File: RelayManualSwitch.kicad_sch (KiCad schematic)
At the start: 10 parts

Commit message: 階層基板化中
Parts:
- removed SW?: SW_DPDT_x2, symbol Switch:SW_DPDT_x2
- removed SW?: SW_DPDT_x2, Button_Switch_THT:SW_E-Switch_EG1271_DPDT, symbol Switch:SW_DPDT_x2
- added RN2-1, RN2-2: 2.2k, Resistor_THT:R_Array_SIP9, symbol Device:R_Network08_US
- added SW2-1, SW2-2, SW2-3, SW2-4, SW2-5, SW2-6, SW2-7, SW2-8: SW_SPST, symbol Switch:SW_SPST
- added SW2-9: 2MD1-T2-B4-M2-Q-N, symbol Switch:SW_DPDT_x2
- gave numbers to parts that had none: 8
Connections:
- net OUTPUT1: now also U2-1.6, U2-1.7
- net OUTPUT2: now also U2-2.6, U2-2.7
- net OUTPUT3: now also U2-3.6, U2-3.7
- net OUTPUT5: now also U2-5.6, U2-5.7
- net OUTPUT6: now also U2-6.6, U2-6.7
- net OUTPUT7: now also U2-7.6, U2-7.7
- net OUTPUT8: now also U2-8.6, U2-8.7
- net at U2-4.5: now also SW2-4.1 (A)
- net at U2-4.6: now also U2-4.7
- net at U2-5.5: now also SW2-5.1 (A)
- net at U2-8.5: now also SW2-8.1 (A)
- net at U2-6.5: now also SW2-6.1 (A)
- net at U2-2.5: now also SW2-2.1 (A)
- net at U2-1.5: now also SW2-1.1 (A)
- net at U2-7.5: now also SW2-7.1 (A)
- net at U2-3.5: now also SW2-3.1 (A)
- new net GND: SW2-1.2 (B), SW2-2.2 (B), SW2-3.2 (B), SW2-4.2 (B), SW2-5.2 (B), SW2-6.2 (B), SW2-7.2 (B), SW2-8.2 (B)
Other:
- note added: "P-00301"
- title: (none) -> Relay Control AUTO/MANUAL
- moved on the sheet: U2-1, U2-2, U2-3, U2-4, U2-5, U2-6, U2-7, U2-8

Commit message: 編集
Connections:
- net +5V: now also SW2-9.1 (A), SW2-9.6 (C)
- net GND: now also SW2-9.3 (C), SW2-9.4 (A), U2-1.2, U2-1.4, U2-2.2, U2-2.4, U2-3.2, U2-3.4, U2-4.2, U2-4.4, U2-5.2, U2-5.4, U2-6.2, U2-6.4, U2-7.2, U2-7.4, U2-8.2, U2-8.4
- net INPUT1: now also U2-1.8
- net INPUT2: now also U2-2.8
- net INPUT3: now also U2-3.8
- net INPUT4: now also U2-4.8
- net INPUT5: now also U2-5.8
- net INPUT6: now also U2-6.8
- net INPUT7: now also U2-7.8
- net INPUT8: now also U2-8.8
- net OUTPUT4: now also U2-4.6, U2-4.7
- net at RN2-1.1 (common): now also SW2-9.2 (B)
- net at RN2-1.2 (R1): now also U2-1.3
- net at RN2-1.3 (R2): now also U2-5.3
- net at RN2-1.4 (R3): now also U2-6.3
- net at RN2-1.5 (R4): now also U2-2.3
- net at RN2-1.6 (R5): now also U2-3.3
- net at RN2-1.7 (R6): now also U2-7.3
- net at RN2-1.8 (R7): now also U2-8.3
- net at RN2-1.9 (R8): now also U2-4.3
- net at U2-4.1: now also RN2-2.9 (R8)
- net at U2-5.1: now also RN2-2.3 (R2)
- net at U2-8.1: now also RN2-2.8 (R7)
- net at U2-6.1: now also RN2-2.4 (R3)
- net at U2-2.1: now also RN2-2.5 (R4)
- net at RN2-2.1 (common): now also SW2-9.5 (B)
- net at RN2-2.2 (R1): now also U2-1.1
- net at RN2-2.6 (R5): now also U2-3.1
- net at RN2-2.7 (R6): now also U2-7.1
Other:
- moved on the sheet: RN2-1, RN2-2, SW2-9A, SW2-9B

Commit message: RelayManualSwitch回路充実
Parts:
- added D2-1, D2-2: LED, symbol Device:LED
- added R2-1, R2-2: 510, symbol Device:R_US
- SW2-9: value 2MD1-T2-B4-M2-Q-N -> MS611F
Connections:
- net GND: now also D2-1.1 (K), D2-2.1 (K)
- net at RN2-1.1 (common), SW2-9.2 (B): now also R2-1.1
- net at RN2-2.1 (common), SW2-9.5 (B): now also R2-2.1
- new net: D2-2.2 (A), R2-2.2
- new net: D2-1.2 (A), R2-1.2
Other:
- note added: "AUTO"
- note added: "MANUAL"
- moved on the sheet: SW2-9A, SW2-9B

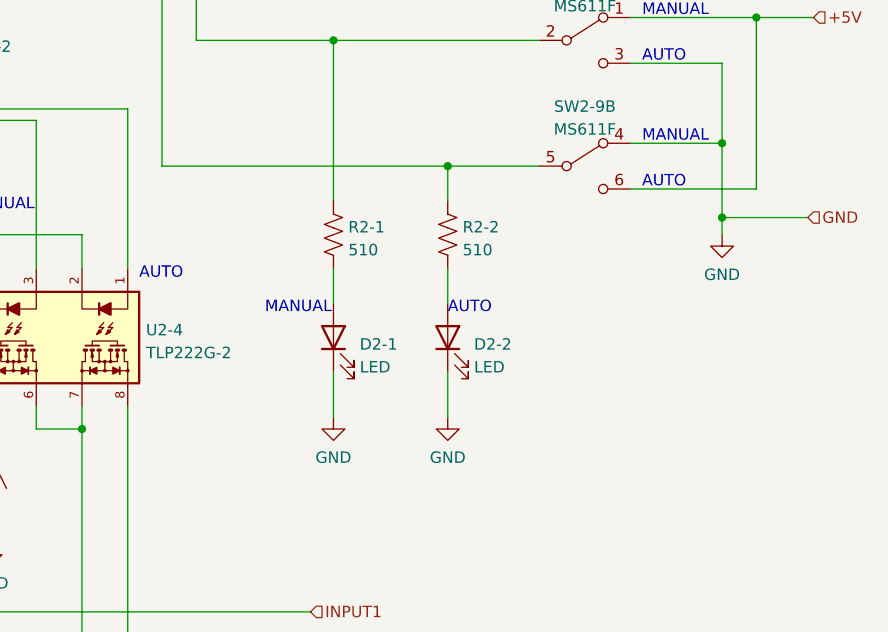
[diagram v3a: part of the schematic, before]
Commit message: Mode STAT monitoring
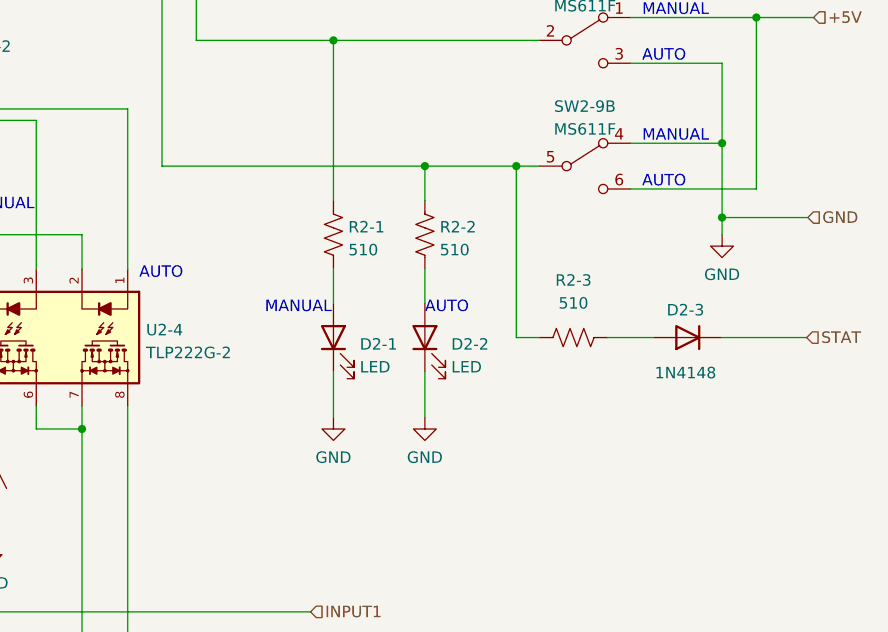
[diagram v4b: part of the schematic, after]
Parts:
- added D2-3: 1N4148, Diode_THT:D_DO-35_SOD27_P7.62mm_Horizontal, symbol Diode:1N4148
- added R2-3: 510, symbol Device:R_US
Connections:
- net at R2-2.1, RN2-2.1 (common), SW2-9.5 (B): now also R2-3.1
- new net: D2-3.2 (A), R2-3.2
- new net STAT: D2-3.1 (K)
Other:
- moved on the sheet: D2-2, R2-2
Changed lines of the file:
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@@
   (junction (at 106.68 76.2) (diameter 0) (color 0 0 0 0)
   )
-  (junction (at 208.28 46.99) (diameter 0) (color 0 0 0 0)
+  (junction (at 205.74 46.99) (diameter 0) (color 0 0 0 0)
   )
   (junction (at 167.64 76.2) (diameter 0) (color 0 0 0 0)
@@
   (junction (at 127 116.84) (diameter 0) (color 0 0 0 0)
   )
+  (junction (at 215.9 46.99) (diameter 0) (color 0 0 0 0)
+  )
   (junction (at 96.52 116.84) (diameter 0) (color 0 0 0 0)
   )
@@
     (stroke (width 0) (type default) (color 0 0 0 0))
   )
+  (wire (pts (xy 238.76 66.04) (xy 248.158 66.04))
+    (stroke (width 0) (type default) (color 0 0 0 0))
+  )
   (wire (pts (xy 146.05 109.22) (xy 132.08 109.22))
     (stroke (width 0) (type default) (color 0 0 0 0))
@@
     (stroke (width 0) (type default) (color 0 0 0 0))
   )
-  (wire (pts (xy 208.28 46.99) (xy 176.53 46.99))
+  (wire (pts (xy 205.74 46.99) (xy 176.53 46.99))
     (stroke (width 0) (type default) (color 0 0 0 0))
   )
@@
     (stroke (width 0) (type default) (color 0 0 0 0))
   )
+  (wire (pts (xy 218.44 66.04) (xy 215.9 66.04))
+    (stroke (width 0) (type default) (color 0 0 0 0))
+  )
   (wire (pts (xy 66.04 118.11) (xy 76.2 118.11))
     (stroke (width 0) (type default) (color 0 0 0 0))
@@
     (stroke (width 0) (type default) (color 0 0 0 0))
   )
+  (wire (pts (xy 215.9 46.99) (xy 205.74 46.99))
+    (stroke (width 0) (type default) (color 0 0 0 0))
+  )
   (wire (pts (xy 95.25 44.45) (xy 146.05 44.45))
     (stroke (width 0) (type default) (color 0 0 0 0))
@@
     (stroke (width 0) (type default) (color 0 0 0 0))
   )
-  (wire (pts (xy 208.28 46.99) (xy 208.28 50.8))
+  (wire (pts (xy 205.74 46.99) (xy 205.74 50.8))
     (stroke (width 0) (type default) (color 0 0 0 0))
   )
@@
     (stroke (width 0) (type default) (color 0 0 0 0))
   )
+  (wire (pts (xy 215.9 66.04) (xy 215.9 46.99))
+    (stroke (width 0) (type default) (color 0 0 0 0))
+  )
   (wire (pts (xy 144.78 39.37) (xy 144.78 57.15))
     (stroke (width 0) (type default) (color 0 0 0 0))
@@
     (stroke (width 0) (type default) (color 0 0 0 0))
   )
+  (wire (pts (xy 226.06 66.04) (xy 231.14 66.04))
+    (stroke (width 0) (type default) (color 0 0 0 0))
+  )
   (wire (pts (xy 167.894 139.7) (xy 167.64 137.16))
     (stroke (width 0) (type default) (color 0 0 0 0))
@@
     (stroke (width 0) (type default) (color 0 0 0 0))
   )
-  (wire (pts (xy 208.28 69.85) (xy 208.28 74.93))
+  (wire (pts (xy 205.74 69.85) (xy 205.74 74.93))
     (stroke (width 0) (type default) (color 0 0 0 0))
   )
@@
     (stroke (width 0) (type default) (color 0 0 0 0))
   )
-  (wire (pts (xy 208.28 58.42) (xy 208.28 62.23))
+  (wire (pts (xy 205.74 58.42) (xy 205.74 62.23))
     (stroke (width 0) (type default) (color 0 0 0 0))
   )
@@
     (stroke (width 0) (type default) (color 0 0 0 0))
   )
-  (wire (pts (xy 218.44 46.99) (xy 208.28 46.99))
+  (wire (pts (xy 218.44 46.99) (xy 215.9 46.99))
     (stroke (width 0) (type default) (color 0 0 0 0))
   )
@@
     (stroke (width 0) (type default) (color 0 0 0 0))
   )
-  (text "AUTO" (at 208.28 63.5 0)
+  (text "AUTO" (at 205.74 63.5 0)
     (effects (font (size 1.27 1.27)) (justify left bottom))
   )
@@
   (hierarchical_label "OUTPUT6" (shape output) (at 50.8 165.1 180)
     (effects (font (size 1.27 1.27)) (justify right))
+  )
+  (hierarchical_label "STAT" (shape input) (at 248.158 66.04 0)
+    (effects (font (size 1.27 1.27)) (justify left))
   )
   (hierarchical_label "OUTPUT2" (shape output) (at 50.8 101.6 180)
@@
     (pin "1")
   )
-  (symbol (lib_id "Device:LED") (at 208.28 66.04 90) (unit 1)
-    (in_bom yes) (on_board yes) (fields_autoplaced)
-    (property "Reference" "D2-2" (id 0) (at 211.201 66.7928 90)
+  (symbol (lib_id "Device:LED") (at 205.74 66.04 90) (unit 1)
+    (in_bom yes) (on_board yes) (fields_autoplaced)
+    (property "Reference" "D2-2" (id 0) (at 208.661 66.7928 90)
       (effects (font (size 1.27 1.27)) (justify right))
     )
-    (property "Value" "LED" (id 1) (at 211.201 69.3297 90)
+    (property "Value" "LED" (id 1) (at 208.661 69.3297 90)
       (effects (font (size 1.27 1.27)) (justify right))
     )
-    (property "Footprint" "" (id 2) (at 208.28 66.04 0)
-      (effects (font (size 1.27 1.27)) hide)
-    )
-    (property "Datasheet" "~" (id 3) (at 208.28 66.04 0)
-      (effects (font (size 1.27 1.27)) hide)
-    )
-    (pin "1")
-    (pin "2")
-  )
-  (symbol (lib_id "Device:R_US") (at 208.28 54.61 0) (unit 1)
-    (in_bom yes) (on_board yes) (fields_autoplaced)
-    (property "Reference" "R2-2" (id 0) (at 209.931 53.7753 0)
-      (effects (font (size 1.27 1.27)) (justify left))
-    )
-    (property "Value" "510" (id 1) (at 209.931 56.3122 0)
-      (effects (font (size 1.27 1.27)) (justify left))
-    )
-    (property "Footprint" "" (id 2) (at 209.296 54.864 90)
-      (effects (font (size 1.27 1.27)) hide)
-    )
-    (property "Datasheet" "~" (id 3) (at 208.28 54.61 0)
+    (property "Footprint" "" (id 2) (at 205.74 66.04 0)
+      (effects (font (size 1.27 1.27)) hide)
+    )
+    (property "Datasheet" "~" (id 3) (at 205.74 66.04 0)
+      (effects (font (size 1.27 1.27)) hide)
+    )
+    (pin "1")
+    (pin "2")
+  )
+  (symbol (lib_id "Device:R_US") (at 205.74 54.61 0) (unit 1)
+    (in_bom yes) (on_board yes) (fields_autoplaced)
+    (property "Reference" "R2-2" (id 0) (at 207.391 53.7753 0)
+      (effects (font (size 1.27 1.27)) (justify left))
+    )
+    (property "Value" "510" (id 1) (at 207.391 56.3122 0)
+      (effects (font (size 1.27 1.27)) (justify left))
+    )
+    (property "Footprint" "" (id 2) (at 206.756 54.864 90)
+      (effects (font (size 1.27 1.27)) hide)
+    )
+    (property "Datasheet" "~" (id 3) (at 205.74 54.61 0)
       (effects (font (size 1.27 1.27)) hide)
     )
@@
     (pin "1")
   )
+  (symbol (lib_id "Diode:1N4148") (at 234.95 66.04 180) (unit 1)
+    (in_bom yes) (on_board yes)
+    (property "Reference" "D2-3" (id 0) (at 234.696 62.992 0))
+    (property "Value" "1N4148" (id 1) (at 234.696 69.977 0))
+    (property "Footprint" "Diode_THT:D_DO-35_SOD27_P7.62mm_Horizontal" (id 2) (at 234.95 61.595 0)
+      (effects (font (size 1.27 1.27)) hide)
+    )
+    (property "Datasheet" "https://assets.nexperia.com/documents/data-sheet/1N4148_1N4448.pdf" (id 3) (at 234.95 66.04 0)
+      (effects (font (size 1.27 1.27)) hide)
+    )
+    (pin "1")
+    (pin "2")
+  )
   (symbol (lib_id "power:GND") (at 91.44 121.92 0) (unit 1)
     (in_bom yes) (on_board yes) (fields_autoplaced)
@@
   (symbol (lib_id "power:GND") (at 195.58 74.93 0) (unit 1)
     (in_bom yes) (on_board yes) (fields_autoplaced)
-    (property "Reference" "#PWR?" (id 0) (at 195.58 81.28 0)
+    (property "Reference" "#PWR0158" (id 0) (at 195.58 81.28 0)
       (effects (font (size 1.27 1.27)) hide)
     )
@@
     (pin "1")
   )
-  (symbol (lib_id "power:GND") (at 208.28 74.93 0) (unit 1)
-    (in_bom yes) (on_board yes) (fields_autoplaced)
-    (property "Reference" "#PWR?" (id 0) (at 208.28 81.28 0)
-      (effects (font (size 1.27 1.27)) hide)
-    )
-    (property "Value" "GND" (id 1) (at 208.28 79.3734 0))
-    (property "Footprint" "" (id 2) (at 208.28 74.93 0)
-      (effects (font (size 1.27 1.27)) hide)
-    )
-    (property "Datasheet" "" (id 3) (at 208.28 74.93 0)
+  (symbol (lib_id "power:GND") (at 205.74 74.93 0) (unit 1)
+    (in_bom yes) (on_board yes) (fields_autoplaced)
+    (property "Reference" "#PWR0159" (id 0) (at 205.74 81.28 0)
+      (effects (font (size 1.27 1.27)) hide)
+    )
+    (property "Value" "GND" (id 1) (at 205.74 79.3734 0))
+    (property "Footprint" "" (id 2) (at 205.74 74.93 0)
+      (effects (font (size 1.27 1.27)) hide)
+    )
+    (property "Datasheet" "" (id 3) (at 205.74 74.93 0)
       (effects (font (size 1.27 1.27)) hide)
     )
@@
       (effects (font (size 1.27 1.27)) hide)
     )
+    (pin "1")
+    (pin "2")
+  )
+  (symbol (lib_id "Device:R_US") (at 222.25 66.04 90) (unit 1)
+    (in_bom yes) (on_board yes) (fields_autoplaced)
+    (property "Reference" "R2-3" (id 0) (at 222.25 59.69 90))
+    (property "Value" "510" (id 1) (at 222.25 62.23 90))
+    (property "Footprint" "" (id 2) (at 222.504 65.024 90)
+      (effects (font (size 1.27 1.27)) hide)
+    )
+    (property "Datasheet" "~" (id 3) (at 222.25 66.04 0)
+      (effects (font (size 1.27 1.27)) hide)
+    )

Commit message: PCB Design start
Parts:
- D2-1, D2-2: footprint (none) -> LED_THT:LED_D3.0mm
- R2-1, R2-2, R2-3: footprint (none) -> Resistor_THT:R_Axial_DIN0207_L6.3mm_D2.5mm_P7.62mm_Horizontal
- U2-1, U2-2, U2-3, U2-4, U2-5, U2-6, U2-7, U2-8: footprint (none) -> Akizuki:TLP222A-2
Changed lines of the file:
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@@
       (effects (font (size 1.27 1.27)) (justify right))
     )
-    (property "Footprint" "" (id 2) (at 205.74 66.04 0)
+    (property "Footprint" "LED_THT:LED_D3.0mm" (id 2) (at 205.74 66.04 0)
       (effects (font (size 1.27 1.27)) hide)
     )
@@
       (effects (font (size 1.27 1.27)) (justify left))
     )
-    (property "Footprint" "" (id 2) (at 206.756 54.864 90)
+    (property "Footprint" "Resistor_THT:R_Axial_DIN0207_L6.3mm_D2.5mm_P7.62mm_Horizontal" (id 2) (at 206.756 54.864 90)
       (effects (font (size 1.27 1.27)) hide)
     )
@@
       (effects (font (size 1.27 1.27)) (justify left))
     )
-    (property "Footprint" "" (id 2) (at 179.07 66.04 0)
+    (property "Footprint" "Akizuki:TLP222A-2" (id 2) (at 179.07 66.04 0)
       (effects (font (size 1.27 1.27)) hide)
     )
@@
       (effects (font (size 1.27 1.27)) (justify right))
     )
-    (property "Footprint" "" (id 2) (at 195.58 66.04 0)
+    (property "Footprint" "LED_THT:LED_D3.0mm" (id 2) (at 195.58 66.04 0)
       (effects (font (size 1.27 1.27)) hide)
     )
@@
       (effects (font (size 1.27 1.27)) (justify left))
     )
-    (property "Footprint" "" (id 2) (at 87.63 129.54 0)
+    (property "Footprint" "Akizuki:TLP222A-2" (id 2) (at 87.63 129.54 0)
       (effects (font (size 1.27 1.27)) hide)
     )
@@
       (effects (font (size 1.27 1.27)) (justify left))
     )
-    (property "Footprint" "" (id 2) (at 179.07 129.54 0)
+    (property "Footprint" "Akizuki:TLP222A-2" (id 2) (at 179.07 129.54 0)
       (effects (font (size 1.27 1.27)) hide)
     )
@@
       (effects (font (size 1.27 1.27)) (justify left))
     )
-    (property "Footprint" "" (id 2) (at 196.596 54.864 90)
+    (property "Footprint" "Resistor_THT:R_Axial_DIN0207_L6.3mm_D2.5mm_P7.62mm_Horizontal" (id 2) (at 196.596 54.864 90)
       (effects (font (size 1.27 1.27)) hide)
     )
@@
       (effects (font (size 1.27 1.27)) (justify left))
     )
-    (property "Footprint" "" (id 2) (at 118.11 129.54 0)
+    (property "Footprint" "Akizuki:TLP222A-2" (id 2) (at 118.11 129.54 0)
       (effects (font (size 1.27 1.27)) hide)
     )
@@
     (property "Reference" "R2-3" (id 0) (at 222.25 59.69 90))
     (property "Value" "510" (id 1) (at 222.25 62.23 90))
-    (property "Footprint" "" (id 2) (at 222.504 65.024 90)
+    (property "Footprint" "Resistor_THT:R_Axial_DIN0207_L6.3mm_D2.5mm_P7.62mm_Horizontal" (id 2) (at 222.504 65.024 90)
       (effects (font (size 1.27 1.27)) hide)
     )
@@
       (effects (font (size 1.27 1.27)) (justify left))
     )
-    (property "Footprint" "" (id 2) (at 118.11 66.04 0)
+    (property "Footprint" "Akizuki:TLP222A-2" (id 2) (at 118.11 66.04 0)
       (effects (font (size 1.27 1.27)) hide)
     )
@@
       (effects (font (size 1.27 1.27)) (justify left))
     )
-    (property "Footprint" "" (id 2) (at 87.63 66.04 0)
+    (property "Footprint" "Akizuki:TLP222A-2" (id 2) (at 87.63 66.04 0)
       (effects (font (size 1.27 1.27)) hide)
     )
@@
       (effects (font (size 1.27 1.27)) (justify left))
     )
-    (property "Footprint" "" (id 2) (at 148.59 129.54 0)
+    (property "Footprint" "Akizuki:TLP222A-2" (id 2) (at 148.59 129.54 0)
       (effects (font (size 1.27 1.27)) hide)
     )
@@
       (effects (font (size 1.27 1.27)) (justify left))
     )
-    (property "Footprint" "" (id 2) (at 148.59 66.04 0)
-      (effects (font (size 1.27 1.27)) hide)
-    )
+    (property "Footprint" "Akizuki:TLP222A-2" (id 2) (at 148.59 66.04 0)
+      (effects (font (size 1.27 1.27)) hide)
+    )

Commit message: UECS/MANUAL 切り替え表示LED
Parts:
- SW2-1, SW2-2, SW2-3, SW2-4, SW2-5, SW2-6, SW2-7, SW2-8: value SW_SPST -> SW_SPDT; footprint (none) -> Akizuki:2MS1T1B4M2QES; symbol Switch:SW_SPST -> Switch:SW_SPDT
- SW2-9: footprint (none) -> Akizuki:2MD1T2B4M2QNS
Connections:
- net GND: now also SW2-1.1 (A), SW2-2.1 (A), SW2-3.1 (A), SW2-4.1 (A), SW2-5.1 (A), SW2-6.1 (A), SW2-7.1 (A), SW2-8.1 (A); no longer SW2-1.2 (B), SW2-2.2 (B), SW2-3.2 (B), SW2-4.2 (B), SW2-5.2 (B), SW2-6.2 (B), SW2-7.2 (B), SW2-8.2 (B)
- net at U2-6.5: now also SW2-6.2 (B); no longer SW2-6.1 (A)
- net at U2-4.5: now also SW2-4.2 (B); no longer SW2-4.1 (A)
- net at U2-7.5: now also SW2-7.2 (B); no longer SW2-7.1 (A)
- net at U2-5.5: now also SW2-5.2 (B); no longer SW2-5.1 (A)
- net at U2-8.5: now also SW2-8.2 (B); no longer SW2-8.1 (A)
- net at U2-2.5: now also SW2-2.2 (B); no longer SW2-2.1 (A)
- net at U2-1.5: now also SW2-1.2 (B); no longer SW2-1.1 (A)
- net at U2-3.5: now also SW2-3.2 (B); no longer SW2-3.1 (A)
- no-connect marks 0 -> 8

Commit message: parts list 更新
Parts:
- D2-3: AKICODE (none) -> I-00743
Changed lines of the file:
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@@
+      (effects (font (size 1.27 1.27)) hide)
+    )
+    (property "AKICODE" "I-00743" (id 4) (at 234.95 66.04 0)
       (effects (font (size 1.27 1.27)) hide)
     )
